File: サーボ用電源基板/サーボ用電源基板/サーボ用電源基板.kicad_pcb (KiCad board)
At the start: 2 copper layers, 64.5 x 61.5 mm, 56 parts, among them IC1 TLP291, IC2 TLP291, P1 BATT_IN, P10 MAIN_SW, P2 BATT_IN, P3 OUT_A, P4 OUT_B, P5 EMERGENCY_SIGNAL, P6 12V, P7 12V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

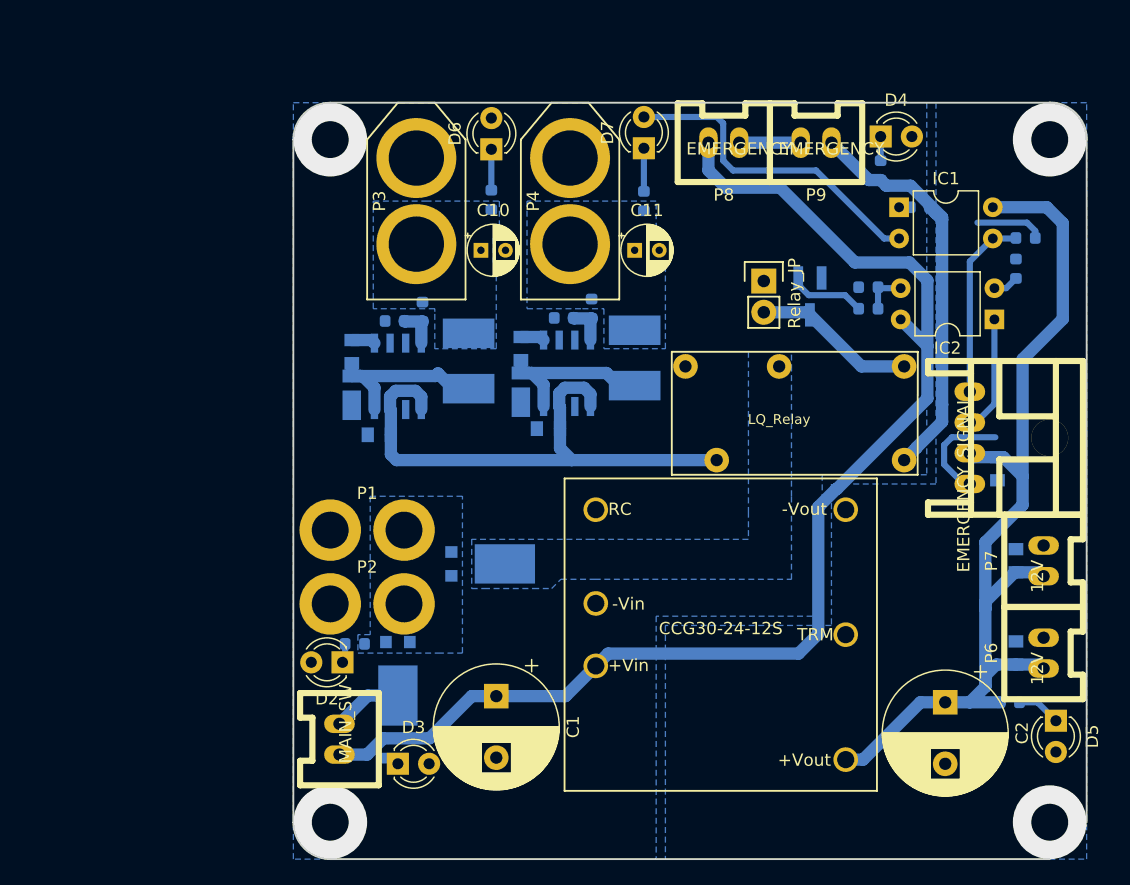
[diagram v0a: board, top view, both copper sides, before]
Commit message: 恐らくエネルギー破壊で燃えた
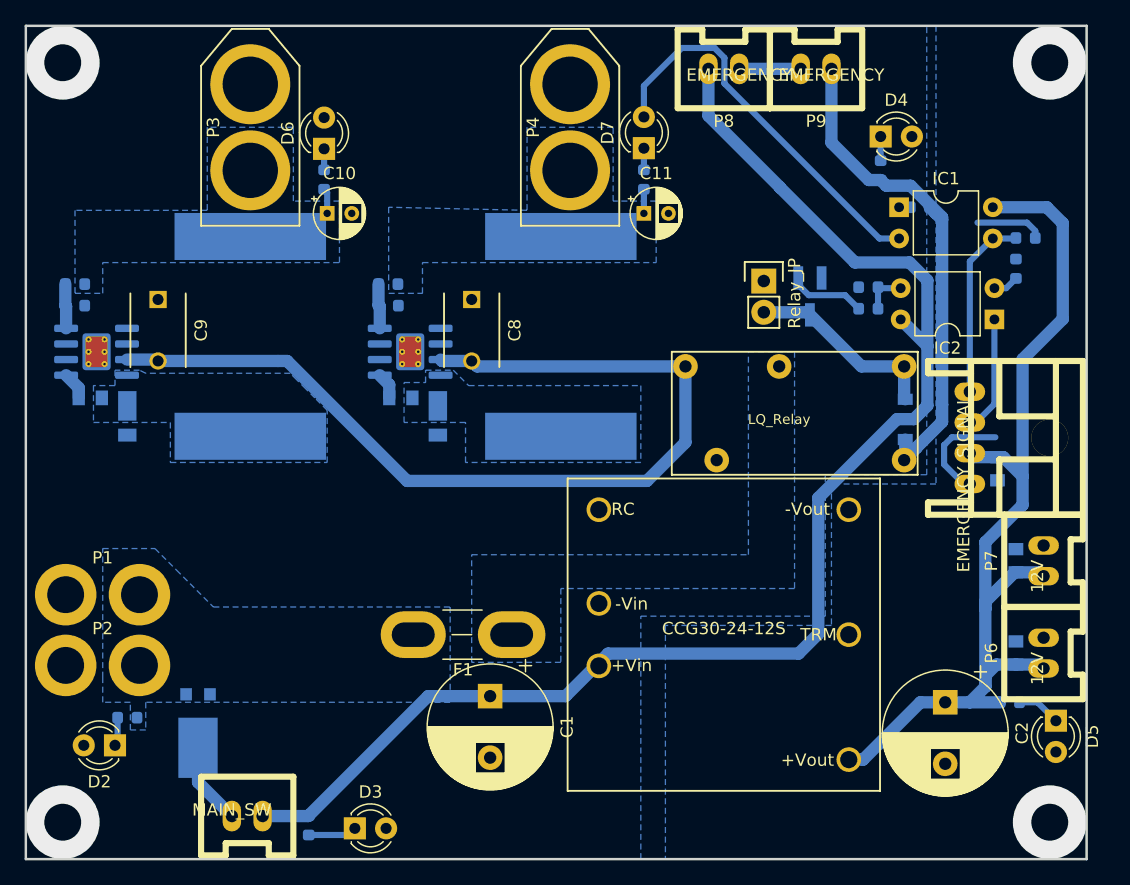
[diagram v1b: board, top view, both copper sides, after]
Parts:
- added F1: FUSE, Fuse:Fuse_Blade_Mini_directSolder, F.Cu at (156.0, 83.0)
- C6, C7: value 10u -> 0.1u
- C8, C9: footprint Capacitors_SMD:C_0603 -> Capacitors_ThroughHole:C_Disc_D6_P5; moved to F.Cu
- D10: value SBR_DIODE -> DIODE; footprint Package_TO_SOT_SMD:TO-277B -> Mizz_lib:SOD-123
- L1, L2: footprint Mizz_lib:Inductor_Taiyo-Yuden_NR-50xx_HandSoldering -> Inductor_SMD:L_Vishay_IHLP-6767
- U3, U4: footprint Mizz_lib:SOIC-8_3.9x4.9mm_Pitch1.27mm -> Package_SO:SOIC-8-1EP_3.9x4.9mm_P1.27mm_EP2.29x3mm_ThermalVias
- moved D10 35.7 mm to (188.0, 65.5), turned to 90 degrees
- moved R12 28.3 mm to (120.5, 54.5), turned to 180 degrees
- moved R13 26.0 mm to (120.5, 56.2), turned to 0 degrees
- moved U3 24.6 mm to (122.2, 60.0), turned to 0 degrees
- moved P1 22.1 mm to (122.7, 79.8)
- moved P2 22.1 mm to (122.7, 85.5)
- moved C6 21.6 mm to (121.8, 63.8), turned to 0 degrees
- moved C9 21.1 mm to (127.2, 55.8), turned to 270 degrees
- moved D2 19.7 mm to (123.8, 92.0)
- moved R6 19.4 mm to (124.8, 89.8)
- moved D8 18.3 mm to (124.8, 65.2), turned to 270 degrees
- moved L1 17.9 mm to (134.8, 58.8)
- moved D1 16.8 mm to (130.5, 91.0)
- moved R14 16.7 mm to (146.0, 54.5), turned to 180 degrees
- moved P3 14.8 mm to (134.8, 41.8)
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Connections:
- D10 pad 1: +BATT -> Relay_BATT
- D10 pad 2: +BATT -> Relay_OUT
- D8 pad 1: GNDPWR -> Net-(C6-Pad2)
- D8 pad 2: Net-(C6-Pad2) -> GNDPWR
- D9 pad 1: GNDPWR -> Net-(C7-Pad2)
- D9 pad 2: Net-(C7-Pad2) -> GNDPWR
- U2 pad 3: Net-(D10-Pad3) -> Net-(F1-Pad1)
- U2 pad 4: Net-(U2-Pad4) -> DCDC_BATT
- U2 pad 5: DCDC_BATT -> Net-(U2-Pad5)
- U3 pad 5: DCDC_BATT -> Net-(U3-Pad5)
- U4 pad 5: DCDC_BATT -> Net-(U4-Pad5)
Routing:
- net DCDC_BATT: track 45.2 -> 77.1 mm
- net Net-(C7-Pad2): track 13.9 -> 0.00 mm
- net 4Cell_BATT: track 102.3 -> 114.8 mm
- net Net-(C6-Pad2): track 14.4 -> 4.25 mm
- net Relay_BATT: track 34.0 -> 41.7 mm
- net GNDPWR: track 26.6 -> 32.2 mm
- net Net-(D3-Pad1): track 1.19 -> 3.97 mm
- net Relay_OUT: track 13.2 -> 15.9 mm
- net 7V_OUTA: track 0.00 -> 2.07 mm
- net 7V_OUTB: track 0.00 -> 1.96 mm
- net Net-(D7-Pad1): track 3.51 -> 1.76 mm
- net Net-(D6-Pad1): track 3.32 -> 1.71 mm
- net Net-(D1-Pad3): track 5.70 -> 6.69 mm
- net Net-(D2-Pad1): track 1.59 -> 2.34 mm
- added copper zone on B.Cu, net Net-(C6-Pad2)
- added copper zone on B.Cu, net Net-(C7-Pad2)
- added copper zone on B.Cu, net Net-(F1-Pad1)
- removed copper zone on B.Cu, net Net-(D10-Pad3)
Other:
- board size 64.5 x 61.5 mm -> 86.2 x 67.8 mm
